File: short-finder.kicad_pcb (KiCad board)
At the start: 2 copper layers, 49 parts, among them J1 USB-MICRO-B, J2 CONN_02X03, J3 CONN_01X02, J4 CONN_01X02, J5 CONN_01X02, J6 CONN_01X02, J7 CONN_01X02, J8 CONN_01X02, P1 CONN_01X03, Q1 PMBT3906,215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

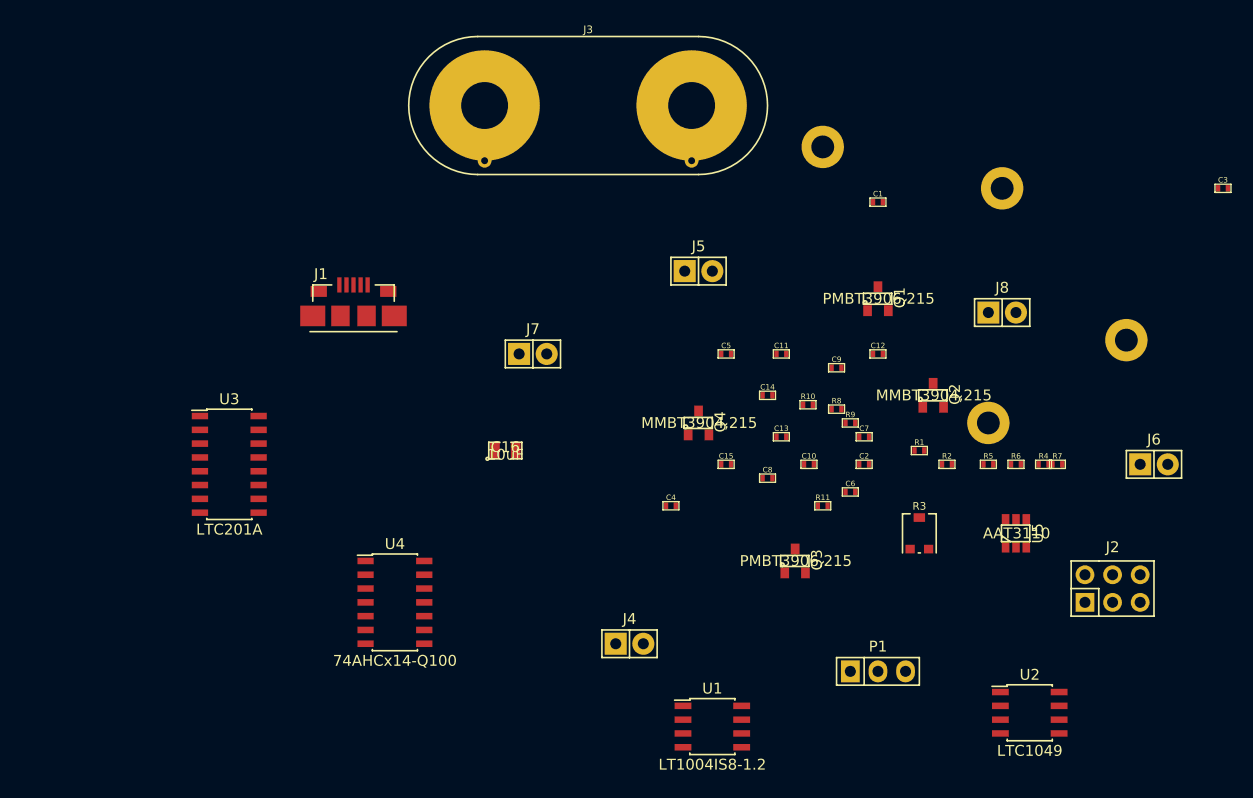
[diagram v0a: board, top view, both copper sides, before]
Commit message: reannotated slightly and started to think about placement
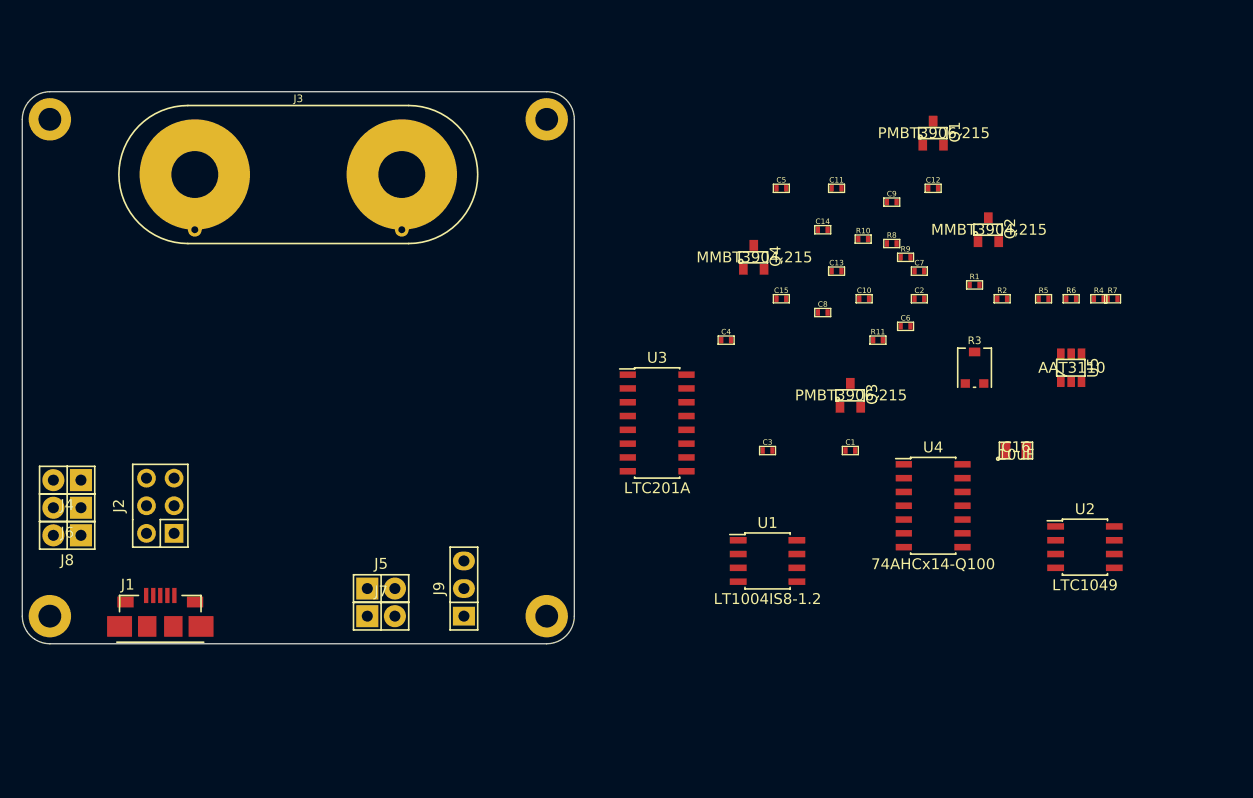
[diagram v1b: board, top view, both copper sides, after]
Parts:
- removed P1: CONN_01X03, Pin_Headers:Pin_Header_Straight_1x03
- added J9: CONN_01X03, Pin_Headers:Pin_Header_Straight_1x03, F.Cu at (116.8, 121.9)
- moved J6 100.1 mm to (80.3, 114.5), turned to 180 degrees
- moved J8 88.4 mm to (80.3, 117.0), turned to 180 degrees
- moved H2 88.2 mm to (78.7, 124.5)
- moved J2 88.0 mm to (88.9, 114.3), turned to 90 degrees
- moved H1 87.9 mm to (78.7, 78.7)
- moved H3 59.1 mm to (124.5, 124.5)
- moved J4 53.9 mm to (80.3, 111.9), turned to 180 degrees
- moved U4 50.3 mm to (160.0, 114.3)
- moved C3 48.4 mm to (144.8, 109.2)
- moved C16 47.0 mm to (167.6, 109.2)
- moved J5 41.3 mm to (109.2, 121.9)
- moved U3 39.6 mm to (134.6, 106.7)
- moved J1 33.7 mm to (88.9, 122.6)
- moved J7 27.9 mm to (109.2, 124.5)
- moved J3 27.4 mm to (101.6, 83.8)
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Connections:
- net Net-(C2-Pad1) renamed /OPAMP_OUT
- net Net-(C2-Pad2) renamed /V-
- net Net-(C4-Pad1) renamed /VREF
- net Net-(C6-Pad1) renamed /SHELL
- net Net-(C7-Pad1) renamed /INV1_IN
- net Net-(C9-Pad1) renamed /D1&2
- net Net-(C9-Pad2) renamed /D2&3
- net Net-(Q1-Pad1) renamed /INV_BASE_DRIVE
- net Net-(Q2-Pad1) renamed /PPP
- net Net-(R1-Pad1) renamed /POT_MID
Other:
- board outline added: 50.8 x 50.8 mm
